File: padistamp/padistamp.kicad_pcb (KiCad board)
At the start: 2 copper layers, 48.3 x 36.8 mm, 8 parts, among them P1 CONN_01X14, P2 CONN_01X14

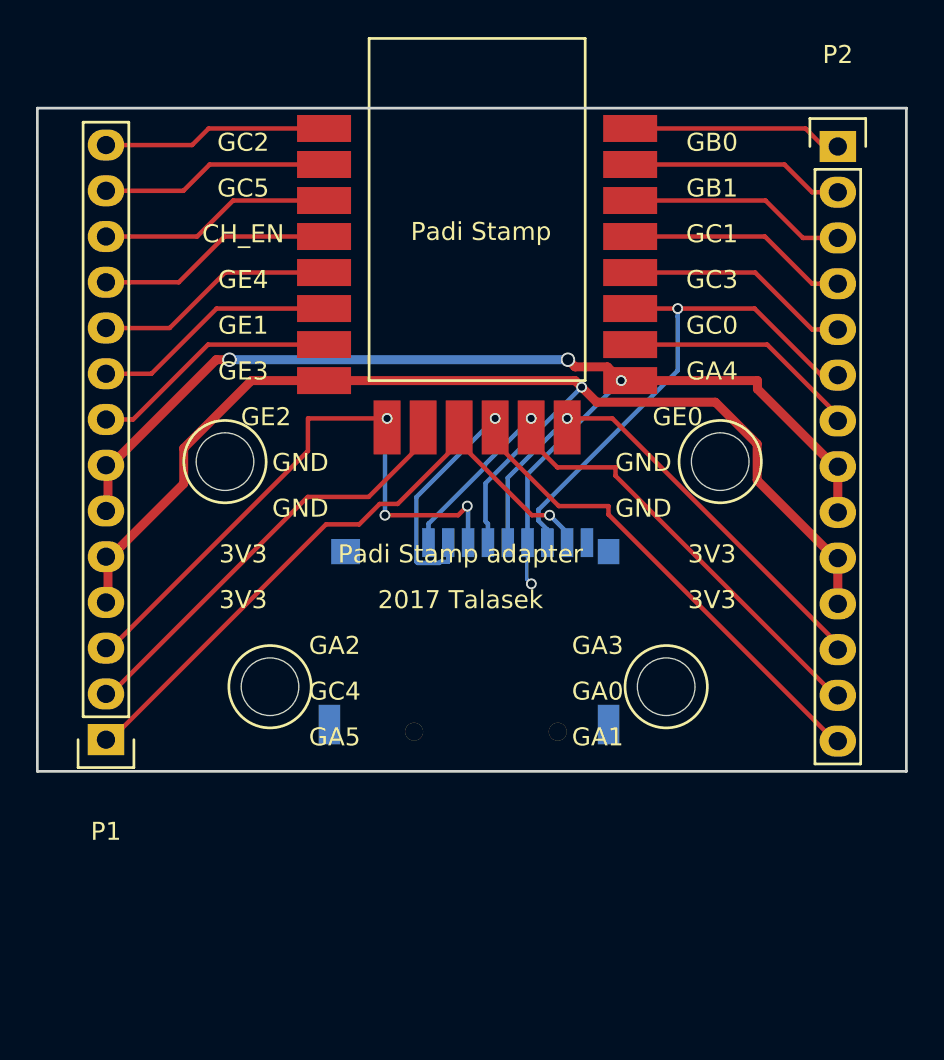
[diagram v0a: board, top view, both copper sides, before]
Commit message: add stabiliser and swd pins
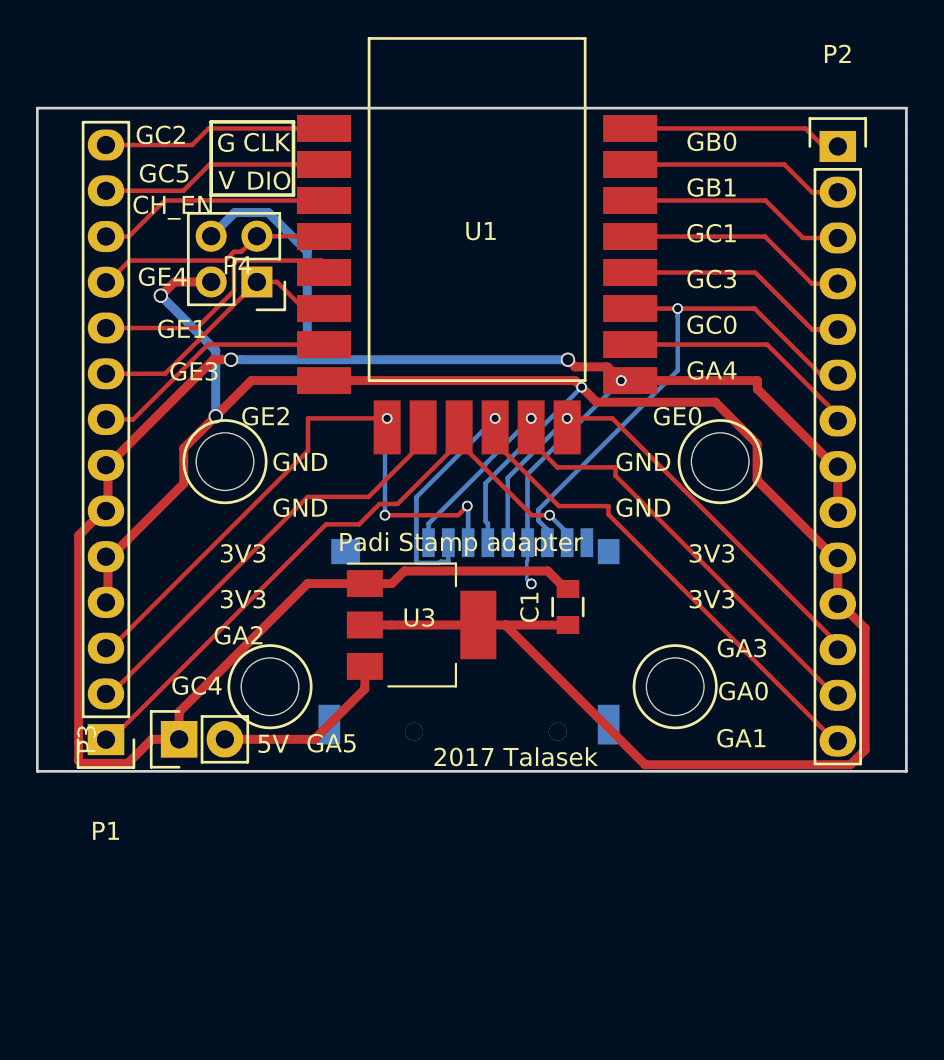
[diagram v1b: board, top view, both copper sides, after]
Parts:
- added C1: 0.1u, Capacitors_SMD:C_0805, F.Cu at (161.5, 130.6)
- added P3: 5V, Pin_Headers:Pin_Header_Straight_1x02, F.Cu at (140.0, 137.9)
- added P4: SWD, Pin_Headers:Pin_Header_Straight_2x02, F.Cu at (144.3, 112.5)
- added U3: TLV1117, TO_SOT_Packages_SMD:SOT-223, F.Cu at (153.4, 131.6)
- U1: renamed from Padi Stamp
- moved REF** 0.50 mm to (167.5, 135.0)
- renumbered microSD to U2
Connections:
- U2 pad 9: Net-(U2-Pad9) -> (no net)
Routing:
- net Net-(C1-Pad2): track 64.5 -> 124.8 mm
- net Net-(C1-Pad1): track 67.1 -> 121.8 mm, vias 1 -> 3
- net Net-(P3-Pad2): track 0.00 -> 10.2 mm
- net Net-(P1-Pad10): track 13.8 -> 15.3 mm
- net Net-(P1-Pad9): track 14.0 -> 15.3 mm
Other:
- board text added: "5V"
- board text added: "CLK"
- board text added: "DIO"
- board text added: "G"
- board text added: "V"

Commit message: not yet done , add serial conn , serial eeprom
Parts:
- removed REF** (x4): 1pin, Connect:1pin
- removed U1: padi_stamp, padistamp:padi_stamp
- added P5: Conn_02x02_Odd_Even, Pin_Headers:Pin_Header_Straight_2x02_Pitch2.54mm, F.Cu at (146.1, 149.8)
- added U5: 25LC_EEPROM, Housings_SOIC:SOIJ-8_5.3x5.3mm_Pitch1.27mm, B.Cu at (156.4, 109.9)
- added padi_stamp1: padi_stamp, padistamp:padi_stamp, F.Cu at (148.6, 104.1)
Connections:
- U2 pad 9: (no net) -> Net-(U2-Pad9)
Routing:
- net Net-(C1-Pad1): track 121.8 -> 138.5 mm
- net Net-(P1-Pad14): track 12.9 -> 27.4 mm, vias 0 -> 1
- net Net-(P2-Pad5): track 13.8 -> 27.1 mm, vias 0 -> 1
- net Net-(P2-Pad4): track 13.6 -> 25.6 mm, vias 0 -> 1
- net Net-(C1-Pad2): track 124.8 -> 134.7 mm
- net Net-(P2-Pad3): track 13.4 -> 18.5 mm, vias 0 -> 1

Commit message: filan
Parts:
- moved P5 50.9 mm to (170.4, 105.0)
- renumbered U5 to Flash, U2 to uSD
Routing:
- net Net-(C1-Pad2): track 134.7 -> 152.5 mm
- net Net-(P2-Pad3): track 18.5 -> 17.9 mm
- net Net-(P2-Pad2): track 13.1 -> 12.5 mm
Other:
- board text added: "B0"
- board text added: "B1"
- board text added: "DBG"
- board text added: "N"
- board text added: "Rx"
- board text added: "Tx"
- board text removed: "GB0"
- board text removed: "GB1"
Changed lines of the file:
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@@
   (general
     (links 58)
-    (no_connects 12)
-    (area 132.004999 102.794999 180.415001 139.775001)
+    (no_connects 4)
+    (area 130.856667 93.45 191.923334 155.720001)
     (thickness 1.6)
-    (drawings 45)
-    (tracks 241)
+    (drawings 55)
+    (tracks 251)
     (zones 0)
     (modules 10)
@@
     (46 B.CrtYd user)
     (47 F.CrtYd user)
-    (48 B.Fab user)
-    (49 F.Fab user)
+    (48 B.Fab user hide)
+    (49 F.Fab user hide)
   )
   (setup
@@
   (module padistamp:uSD (layer B.Cu)
     (at 156.05 126.2 180)
-    (fp_text reference U2 (at 0 -6.7 180) (layer B.SilkS)
+    (fp_text reference uSD (at -3.081 -8.166 180) (layer B.SilkS)
       (effects (font (size 1 1) (thickness 0.15)) (justify mirror))
     )
-    (fp_text value uSD (at 0 -3.95 180) (layer B.Fab)
+    (fp_text value uSD (at -0.033 -2.832 180) (layer B.Fab)
       (effects (font (size 1 1) (thickness 0.15)) (justify mirror))
     )
@@
   (module padistamp:padi_stamp (layer F.Cu)
     (at 148.59 104.14)
-    (fp_text reference padi_stamp1 (at 6.3 11.3) (layer F.SilkS)
+    (fp_text reference padi_stamp1 (at 8.001 11.684) (layer F.SilkS)
       (effects (font (size 1 1) (thickness 0.15)))
     )
@@
   )
   (module Pin_Headers:Pin_Header_Straight_2x02_Pitch2.54mm (layer F.Cu)
-    (at 146.05 149.775001)
+    (at 170.3705 105.029)
     (descr "Through hole straight pin header, 2x02, 2.54mm pitch, double rows")
     (tags "Through hole pin header THT 2x02 2.54mm double row")
@@
     (tags "SOIC 1.27")
     (attr smd)
-    (fp_text reference U5 (at 0 3.68) (layer B.SilkS)
+    (fp_text reference Flash (at 0 3.68) (layer B.SilkS)
       (effects (font (size 1 1) (thickness 0.15)) (justify mirror))
     )
@@
     )
   )
+  (gr_line (start 171.196 108.966) (end 171.577 121.031) (layer F.SilkS) (width 0.2))
+  (gr_line (start 169.037 124.841) (end 169.037 121.031) (layer F.SilkS) (width 0.2))
+  (gr_line (start 173.101 124.841) (end 169.037 124.841) (layer F.SilkS) (width 0.2))
+  (gr_line (start 173.101 121.031) (end 173.101 124.841) (layer F.SilkS) (width 0.2))
+  (gr_line (start 169.037 121.031) (end 173.101 121.031) (layer F.SilkS) (width 0.2))
+  (gr_text N (at 169.672 122.047) (layer F.SilkS)
+    (effects (font (size 1 1) (thickness 0.2)))
+  )
+  (gr_text G (at 169.672 124.079) (layer F.SilkS)
+    (effects (font (size 1 1) (thickness 0.2)))
+  )
+  (gr_text Rx (at 171.831 124.079) (layer F.SilkS)
+    (effects (font (size 1 1) (thickness 0.2)))
+  )
+  (gr_text Tx (at 171.831 122.047) (layer F.SilkS)
+    (effects (font (size 1 1) (thickness 0.2)))
+  )
+  (gr_text DBG (at 172.974 110.363) (layer F.SilkS)
+    (effects (font (size 1 1) (thickness 0.2)))
+  )
   (gr_line (start 141.732 107.696) (end 141.732 103.632) (layer F.SilkS) (width 0.2))
   (gr_line (start 146.304 107.696) (end 141.732 107.696) (layer F.SilkS) (width 0.2))
@@
     (effects (font (size 1 1) (thickness 0.2)))
   )
-  (gr_text GB1 (at 169.545 107.315) (layer F.SilkS)
-    (effects (font (size 1 1) (thickness 0.2)))
-  )
-  (gr_text GB0 (at 169.545 104.775) (layer F.SilkS)
+  (gr_text B1 (at 168.021 107.696) (layer F.SilkS)
+    (effects (font (size 1 1) (thickness 0.2)))
+  )
+  (gr_text B0 (at 167.894 104.902) (layer F.SilkS)
     (effects (font (size 1 1) (thickness 0.2)))
   )
@@
   (segment (start 140.672 104.92) (end 136 104.92) (width 0.25) (layer F.Cu) (net 10))
   (segment (start 148.5011 104) (end 141.592 104) (width 0.25) (layer F.Cu) (net 10))
-  (segment (start 164.5011 104) (end 174.734 104) (width 0.25) (layer F.Cu) (net 11))
-  (segment (start 174.734 104) (end 175.734 105) (width 0.25) (layer F.Cu) (net 11))
-  (segment (start 175.734 105) (end 177 105) (width 0.25) (layer F.Cu) (net 11))
-  (segment (start 173.564 106) (end 175.104 107.54) (width 0.25) (layer F.Cu) (net 12))
-  (segment (start 175.104 107.54) (end 177 107.54) (width 0.25) (layer F.Cu) (net 12))
-  (segment (start 164.5011 106) (end 173.564 106) (width 0.25) (layer F.Cu) (net 12))
+  (segment (start 167.418001 103.853999) (end 167.132 104.14) (width 0.25) (layer F.Cu) (net 11))
+  (segment (start 167.132 104.14) (end 164.59 104.14) (width 0.25) (layer F.Cu) (net 11))
+  (segment (start 172.9105 105.029) (end 171.735499 103.853999) (width 0.25) (layer F.Cu) (net 11))
+  (segment (start 171.735499 103.853999) (end 167.418001 103.853999) (width 0.25) (layer F.Cu) (net 11))
+  (segment (start 176.53 105) (end 172.9395 105) (width 0.25) (layer F.Cu) (net 11) (status C00000))
+  (segment (start 172.9395 105) (end 172.9105 105.029) (width 0.25) (layer F.Cu) (net 11) (status C00000))
+  (segment (start 172.9105 107.569) (end 171.545501 106.204001) (width 0.25) (layer F.Cu) (net 12))
+  (segment (start 171.545501 106.204001) (end 164.654001 106.204001) (width 0.25) (layer F.Cu) (net 12))
+  (segment (start 164.654001 106.204001) (end 164.59 106.14) (width 0.25) (layer F.Cu) (net 12))
+  (segment (start 176.53 107.54) (end 172.9395 107.54) (width 0.25) (layer F.Cu) (net 12) (status C00000))
+  (segment (start 172.9395 107.54) (end 172.9105 107.569) (width 0.25) (layer F.Cu) (net 12) (status C00000))
+  (segment (start 168.053001 108.744001) (end 167.449 108.14) (width 0.25) (layer F.Cu) (net 13))
+  (segment (start 167.449 108.14) (end 164.59 108.14) (width 0.25) (layer F.Cu) (net 13))
+  (segment (start 176.53 110.08) (end 175.264 110.08) (width 0.25) (layer F.Cu) (net 13))
+  (segment (start 175.264 110.08) (end 173.928001 108.744001) (width 0.25) (layer F.Cu) (net 13))
+  (segment (start 173.928001 108.744001) (end 168.053001 108.744001) (width 0.25) (layer F.Cu) (net 13))
   (segment (start 163.195 107.95) (end 164.4 107.95) (width 0.25) (layer F.Cu) (net 13))
   (segment (start 164.4 107.95) (end 164.59 108.14) (width 0.25) (layer F.Cu) (net 13))
@@
   (segment (start 161.925 109.22) (end 163.195 107.95) (width 0.25) (layer B.Cu) (net 13))
   (via (at 163.195 107.95) (size 0.6) (drill 0.4) (layers F.Cu B.Cu) (net 13))
-  (segment (start 172.516 108) (end 174.596 110.08) (width 0.25) (layer F.Cu) (net 13))
-  (segment (start 174.596 110.08) (end 177 110.08) (width 0.25) (layer F.Cu) (net 13))
-  (segment (start 164.5011 108) (end 172.516 108) (width 0.25) (layer F.Cu) (net 13))
   (segment (start 156.21 110.49) (end 164.24 110.49) (width 0.25) (layer F.Cu) (net 14))
   (segment (start 164.24 110.49) (end 164.59 110.14) (width 0.25) (layer F.Cu) (net 14))
@@
   (segment (start 143.965998 118) (end 140.208 121.757998) (width 0.5) (layer F.Cu) (net 21))
   (segment (start 140.208 121.757998) (end 140.208 123.7244) (width 0.5) (layer F.Cu) (net 21))
+  (segment (start 170.3705 107.569) (end 170.3705 116.7729) (width 0.25) (layer B.Cu) (net 22))
+  (segment (start 170.3705 116.7729) (end 176.3776 122.78) (width 0.25) (layer B.Cu) (net 22))
+  (segment (start 176.3776 122.78) (end 176.53 122.78) (width 0.25) (layer B.Cu) (net 22))
   (segment (start 147.066 116.84) (end 151.13 116.84) (width 0.5) (layer B.Cu) (net 22))
   (segment (start 151.13 116.84) (end 161.544 116.84) (width 0.5) (layer B.Cu) (net 22))
@@
       )
     )
+  )
+  (zone (net 22) (net_name "Net-(C1-Pad2)") (layer B.Cu) (hatch edge 0.508)
+    (connect_pads (clearance 0.508))
+    (min_thickness 0.254)
+    (fill yes (arc_segments 16) (thermal_gap 0.508) (thermal_bridge_width 0.508))
+    (polygon
+      (pts
+        (xy 132.207 102.87) (xy 180.34 102.87) (xy 180.34 139.7) (xy 132.08 139.7) (xy 132.08 102.87)
+        (xy 132.08 102.87)
+      )
+    )
+  )
+  (zone (net 22) (net_name "Net-(C1-Pad2)") (layer F.Cu) (hatch edge 0.508)
+    (connect_pads (clearance 0.508))
+    (min_thickness 0.254)
+    (fill yes (arc_segments 16) (thermal_gap 0.508) (thermal_bridge_width 0.508))
+    (polygon
+      (pts
+        (xy 132.08 102.87) (xy 180.34 102.87) (xy 180.34 139.7) (xy 132.08 139.7)
+      )
+    )

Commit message: add spaces where need it
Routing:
- net Net-(P1-Pad2): track 24.6 -> 26.1 mm
- net Net-(P1-Pad1): track 36.3 -> 37.7 mm

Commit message: V3 board
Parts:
- added ?: MountingHole_3.2mm_M3, Mounting_Holes:MountingHole_3.2mm_M3, F.Cu at (167.0, 133.3)
- added ?: MountingHole_3.2mm_M3, Mounting_Holes:MountingHole_3.2mm_M3, F.Cu at (146.1, 133.3)
- added ?: MountingHole_3.2mm_M3, Mounting_Holes:MountingHole_3.2mm_M3, F.Cu at (142.9, 122.6)
- Padi Stamp: renamed from padi_stamp1
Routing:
- added copper zone on B.Cu, net Net-(C1-Pad1)
- added copper zone on F.Cu, net Net-(C1-Pad1)
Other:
- board text added: "2018 Talasek"
- board text added: "A0/0"
- board text added: "A1/1"
- board text added: "A2/2"
- board text added: "A3/3"
- board text added: "A4/4"
- board text added: "A5/5"
- board text added: "C0/8"
- board text added: "C1/9"
- board text added: "C2/10"
- board text added: "C3/11"
- board text added: "C4/12"
- board text added: "C5/13"
- board text added: "E0/14"
- board text added: "E1/15"
- board text added: "E2/16"
- board text added: "E3/17"
- board text added: "E4/18"
- board text added: "I2C1_SCL"
- board text added: "I2C1_SDA"
- board text added: "RX0"
- board text added: "RX2"
- board text added: "SPI0_CLK"
- board text added: "SPI0_CS0"
- board text added: "SPI0_MISO"
- board text added: "SPI0_MOSI"
- board text added: "TX0"
- board text added: "TX2"
- board text removed: "2017 Talasek"
- board text removed: "GA0"
- board text removed: "GA1"
- board text removed: "GA2"
- board text removed: "GA3"
- board text removed: "GA4"
- board text removed: "GA5"
- board text removed: "GC0"
- board text removed: "GC1"
- board text removed: "GC2"
- board text removed: "GC3"
- board text removed: "GC4"
- board text removed: "GC5"
- board text removed: "GE0"
- board text removed: "GE1"
- board text removed: "GE2"
- board text removed: "GE3"
- board text removed: "GE4"
